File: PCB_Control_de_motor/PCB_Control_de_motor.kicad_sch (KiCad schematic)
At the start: 7 parts

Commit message: Esquemático listo
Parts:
- added Batería1: XT30UPB-M, SamacSys_Parts:SHDR2W160P0X500_1X2_1020X520X1070P, symbol SamacSys_Parts:XT30UPB-M
- renumbered Motor to Motor1, Potenciómetro to Potenciómetro1, R8 to R1, R9 to R2, R11 to R3, R10 to R4, Sensores_Boton to Sensores_Boton1
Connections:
- net GND: now also Batería1.2
- new net +12V: Batería1.1
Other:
- added sheet Alimentación (Conexiones_alimentación.kicad_sch)
- sheet Driver ports: added none; removed VM
- moved on the sheet: Motor1, Potenciómetro1, R1, R2, R3, R4, Sensores_Boton1

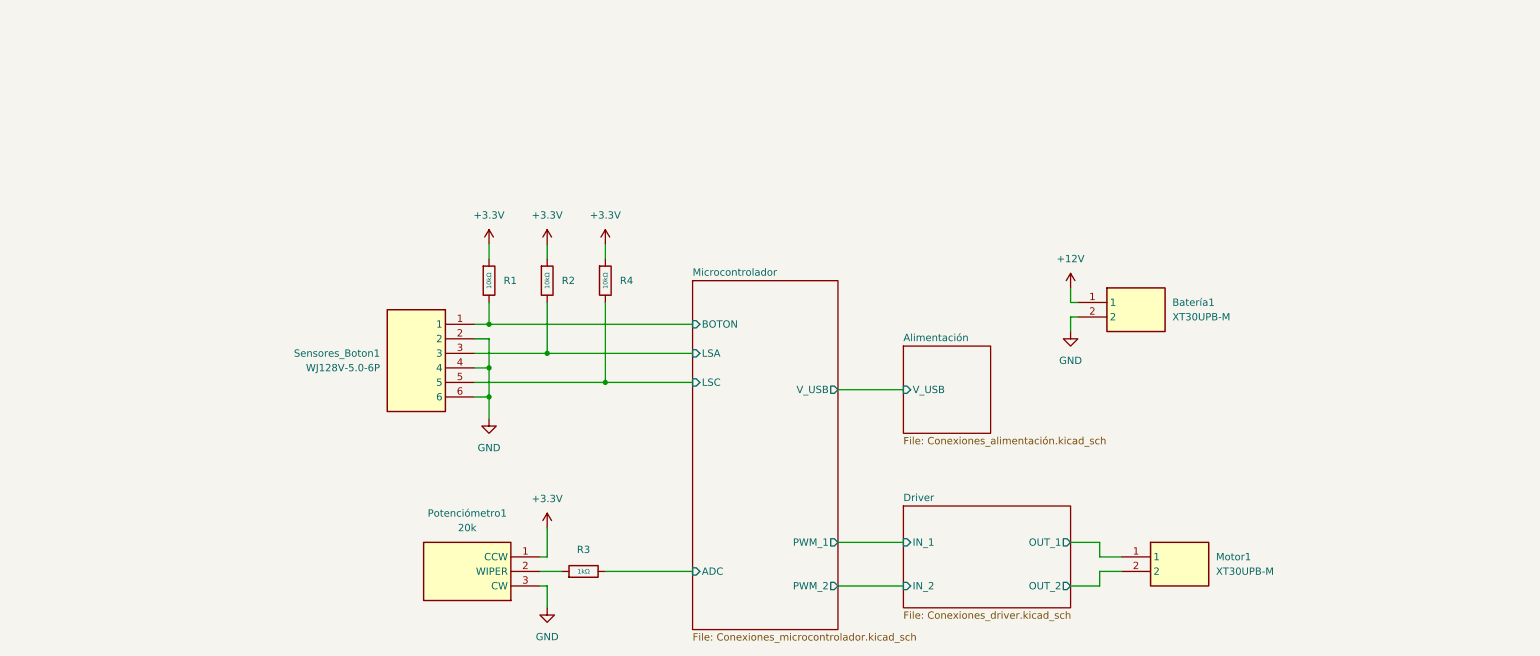
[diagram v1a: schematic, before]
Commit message: Agregado de diodos TVS y avance del PCB con fuente y micro listo
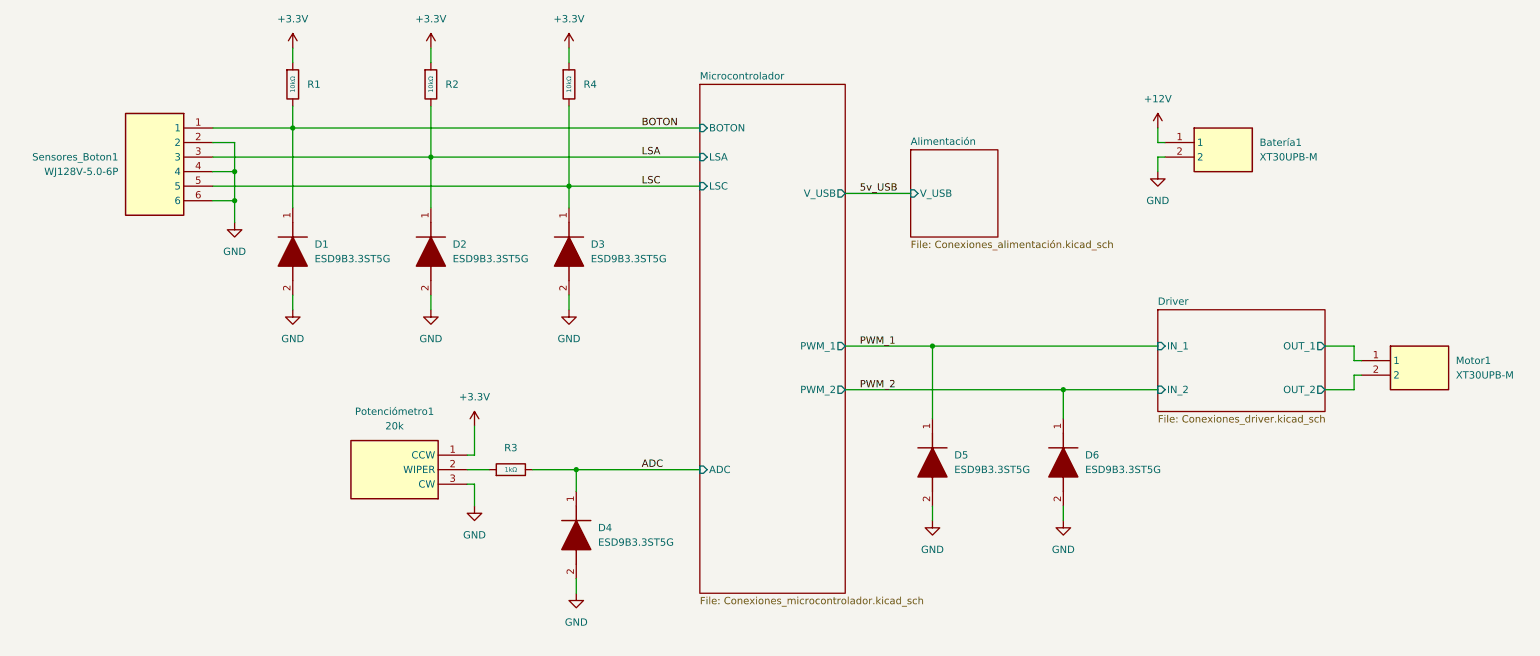
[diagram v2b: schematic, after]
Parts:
- added D1, D2, D3, D4, D5, D6: ESD9B3.3ST5G, SamacSys_Parts:SODFL1006X40N, symbol SamacSys_Parts:ESD9B3.3ST5G
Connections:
- net Driver/IN_1: now also D5.1 (K)
- net Driver/IN_2: now also D6.1 (K)
- net GND: now also D1.2 (A), D2.2 (A), D3.2 (A), D4.2 (A), D5.2 (A), D6.2 (A)
- net Microcontrolador/ADC renamed ADC
- net ADC: now also D4.1 (K)
- net Microcontrolador/BOTON renamed BOTON
- net BOTON: now also D1.1 (K)
- net Microcontrolador/LSA renamed LSA
- net LSA: now also D2.1 (K)
- net Microcontrolador/LSC renamed LSC
- net LSC: now also D3.1 (K)
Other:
- moved on the sheet: Batería1, Motor1, Potenciómetro1, R1, R2, R3, R4, Sensores_Boton1
